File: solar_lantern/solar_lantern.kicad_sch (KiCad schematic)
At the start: 23 parts, among them J1 PV, J2 AVR-ISP-6, SW1 SW_Push, U2 ATtiny441-SS

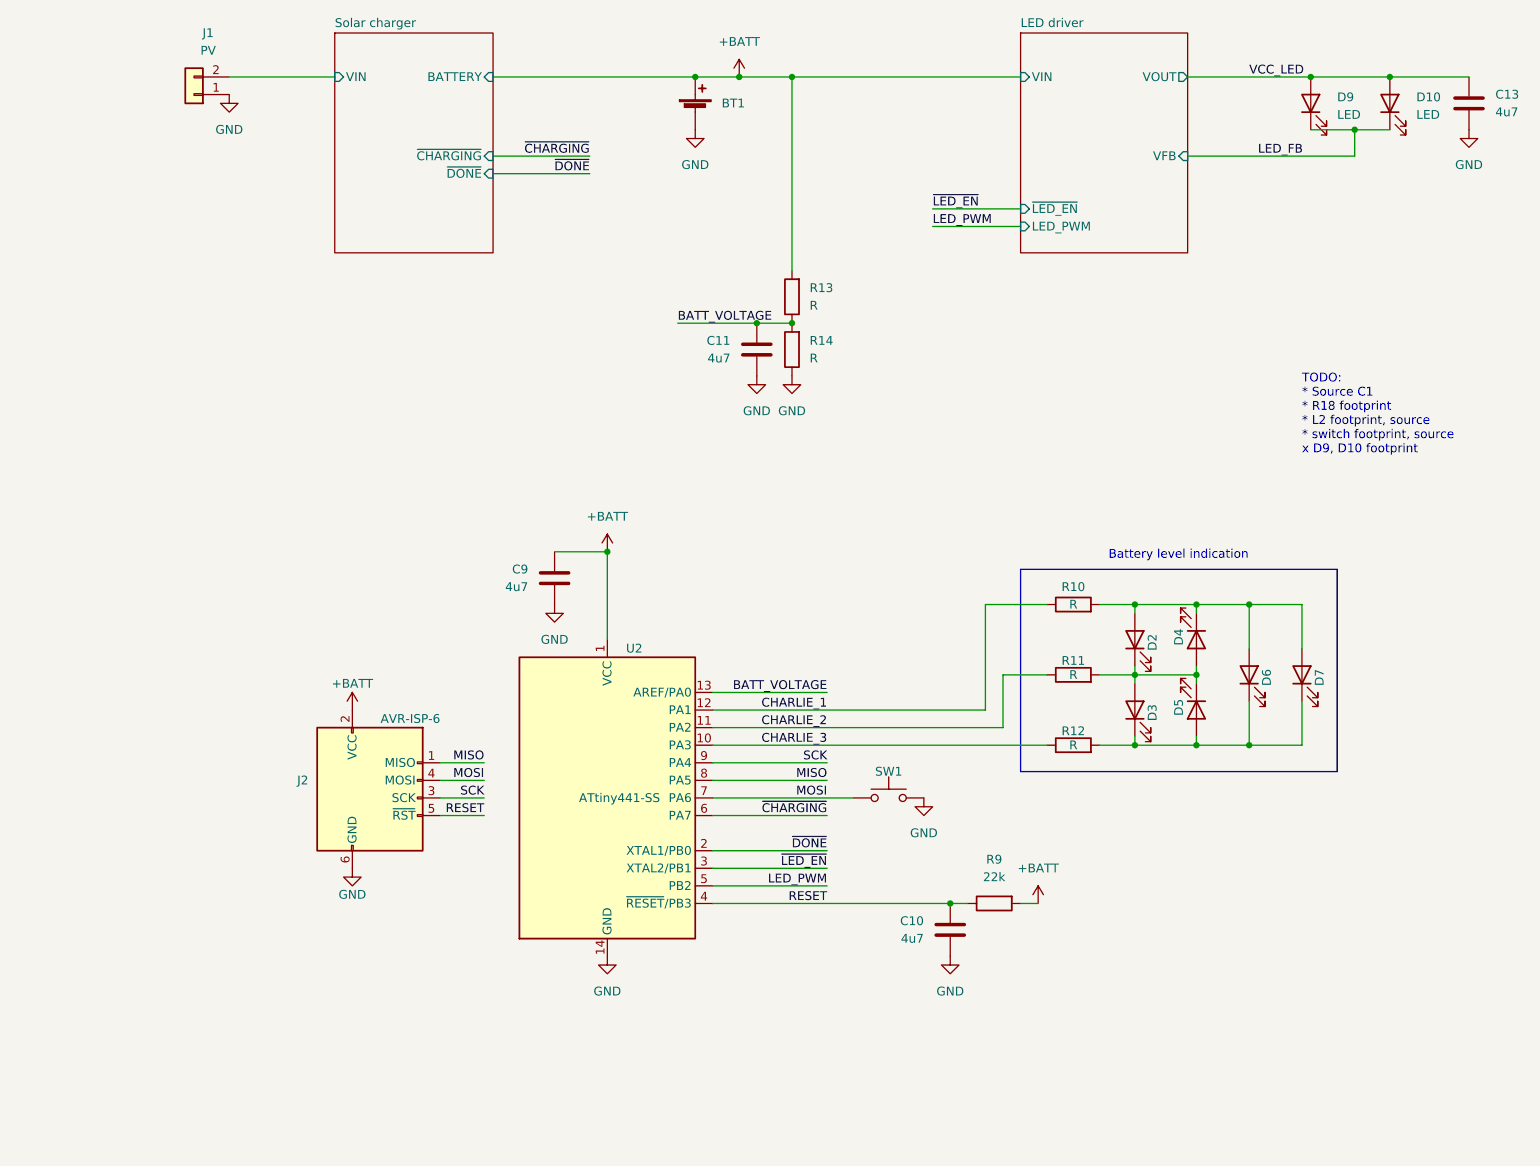
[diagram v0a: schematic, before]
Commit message: Make board smaller, Fix bad cap orientation, Add a diode to reduce quescient current
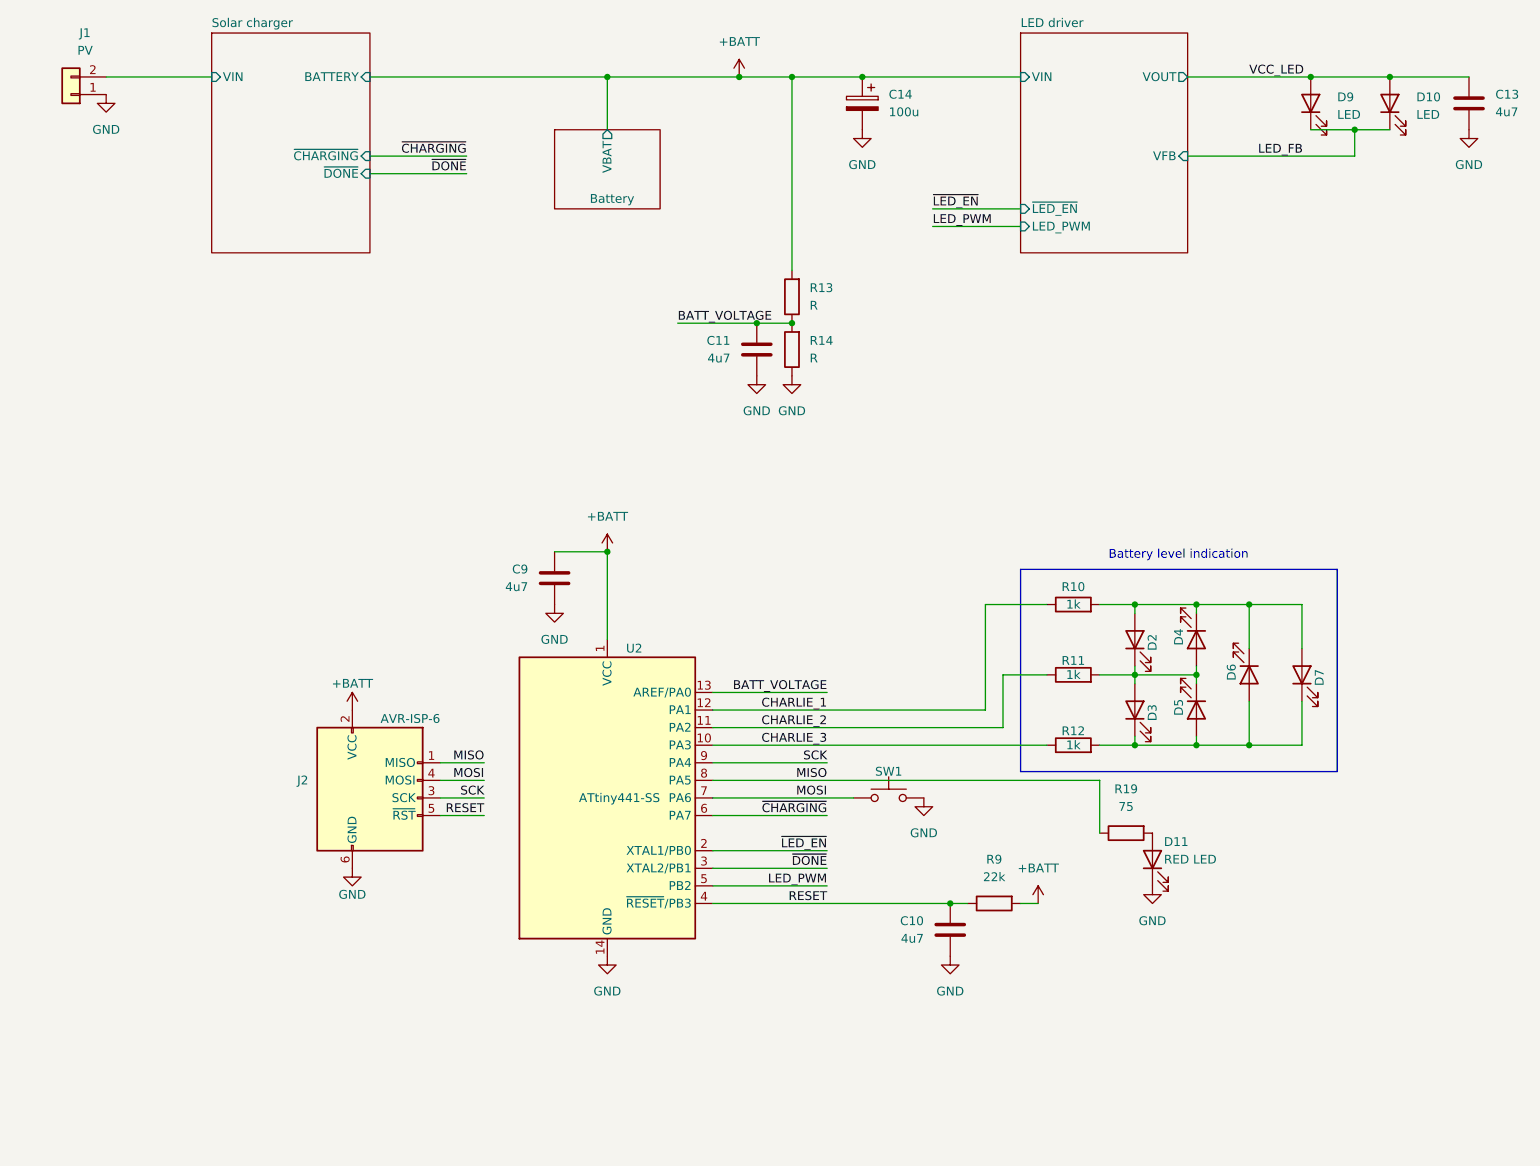
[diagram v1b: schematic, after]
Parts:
- removed BT1: Battery_Cell, Connector_PinHeader_2.54mm:PinHeader_1x02_P2.54mm_Vertical, symbol Device:Battery_Cell
- added C14: 100u, Capacitor_SMD:CP_Elec_6.3x5.4_Nichicon, symbol Device:C_Polarized
- added D11: RED LED, LED_SMD:LED_PLCC-2, symbol Device:LED
- added R19: 75, Resistor_SMD:R_0603_1608Metric, symbol Device:R
- R10, R11, R12: value R -> 1k
- SW1: Manufacturer (none) -> TE Connectivity; PartNo (none) -> 1571407-2
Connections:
- net +BATT: now also C14.1
- net GND: now also C14.2, D11.2 (K)
- net MISO: now also R19.1
- net ~{DONE}: now also U2.3 (XTAL2/PB1); no longer U2.2 (XTAL1/PB0)
- net ~{LED_EN}: now also U2.2 (XTAL1/PB0); no longer U2.3 (XTAL2/PB1)
- net at D3.1 (K), D5.2 (A), D7.1 (K)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: now also D6.2 (A); no longer D6.1 (K)
- net at D2.2 (A), D4.1 (K), D7.2 (A)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: now also D6.1 (K); no longer D6.2 (A)
- new net: D11.1 (A), R19.2
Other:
- added sheet Battery (battery.kicad_sch)
- note removed: "TODO: * Source C1 * R18 footprint * L2 footprint, source * switch footprint, source x D9, D10 footprint"
- moved on the sheet: D6, J1

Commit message: Nicen schematics a bit
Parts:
- D10, D9: PartNo (none) -> L130-4070003000W21
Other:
- company: (none) -> Catnip electronics
- title: (none) -> Solar Camping Lantern

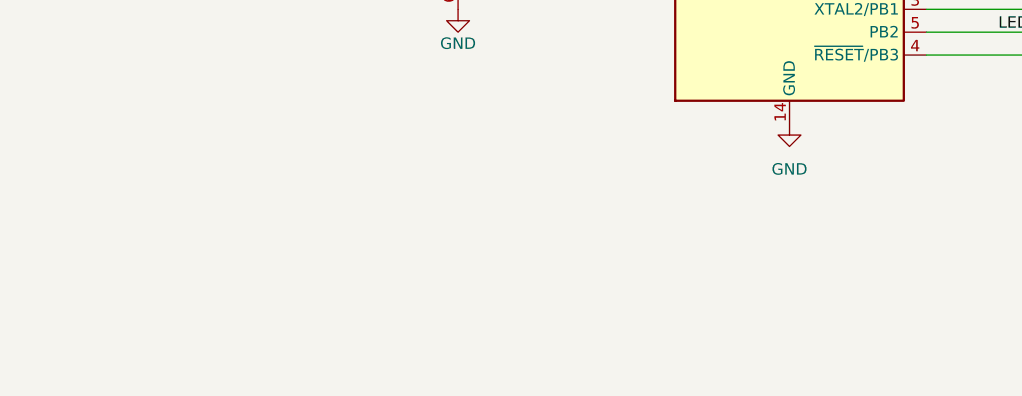
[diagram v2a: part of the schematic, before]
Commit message: Add CERN-OHL_S licence
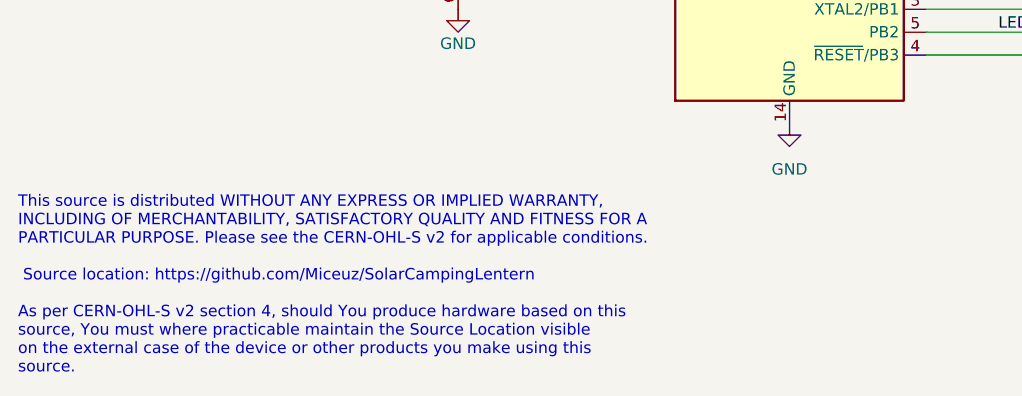
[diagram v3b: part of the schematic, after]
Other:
- note added: "This source is distributed WITHOUT ANY EXPRESS OR IMPLIED WARRANTY, INCLUDING OF MERCHANTABILITY, SATISFACTORY QUALITY AND FITNESS FOR A PARTICULAR PURPOSE. Please see the CERN-OHL-S v2 for applicable conditions. Source location: https://github.com/Miceuz/SolarCampingLentern As per CERN-OHL-S v2 section 4, should You produce hardware based on this source, You must where practicable maintain the S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"
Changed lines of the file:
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@@
     (comment 1 "Albertas Mickėnas")
     (comment 2 "mic@wemakethings.net")
+    (comment 3 "SPDX-License-Identifier: CERN-OHL-S-2.0")
   )
   (junction (at 182.88 121.92) (diameter 0) (color 0 0 0 0)
@@
     (stroke (width 0) (type default))
   )
+  (text "This source is distributed WITHOUT ANY EXPRESS OR IMPLIED WARRANTY,          \nINCLUDING OF MERCHANTABILITY, SATISFACTORY QUALITY AND FITNESS FOR A         \nPARTICULAR PURPOSE. Please see the CERN-OHL-S v2 for applicable conditions.  \n                                                                              \n Source location: https://github.com/Miceuz/SolarCampingLentern\n                                                                              \nAs per CERN-OHL-S v2 section 4, should You produce hardware based on this    \nsource, You must where practicable maintain the Source Location visible      \non the external case of the device or other products you make using this      \nsource.                                                                      \n"
+    (at 20.955 190.5 0)
+    (effects (font (size 1.27 1.27)) (justify left bottom))
+  )
   (text "Battery level indication" (at 179.07 105.41 0)
